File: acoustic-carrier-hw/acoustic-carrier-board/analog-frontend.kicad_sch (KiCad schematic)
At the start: 101 parts, among them J1001 BWU.FL-IPEX1, J1002 BWU.FL-IPEX1, J1003 BWU.FL-IPEX1, J1004 BWU.FL-IPEX1, J1005 BWU.FL-IPEX1, J1006 BWU.FL-IPEX1, J1007 8P8C_Shielded, J1008 BWU.FL-IPEX1, J1009 BWU.FL-IPEX1, J1010 BWU.FL-IPEX1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

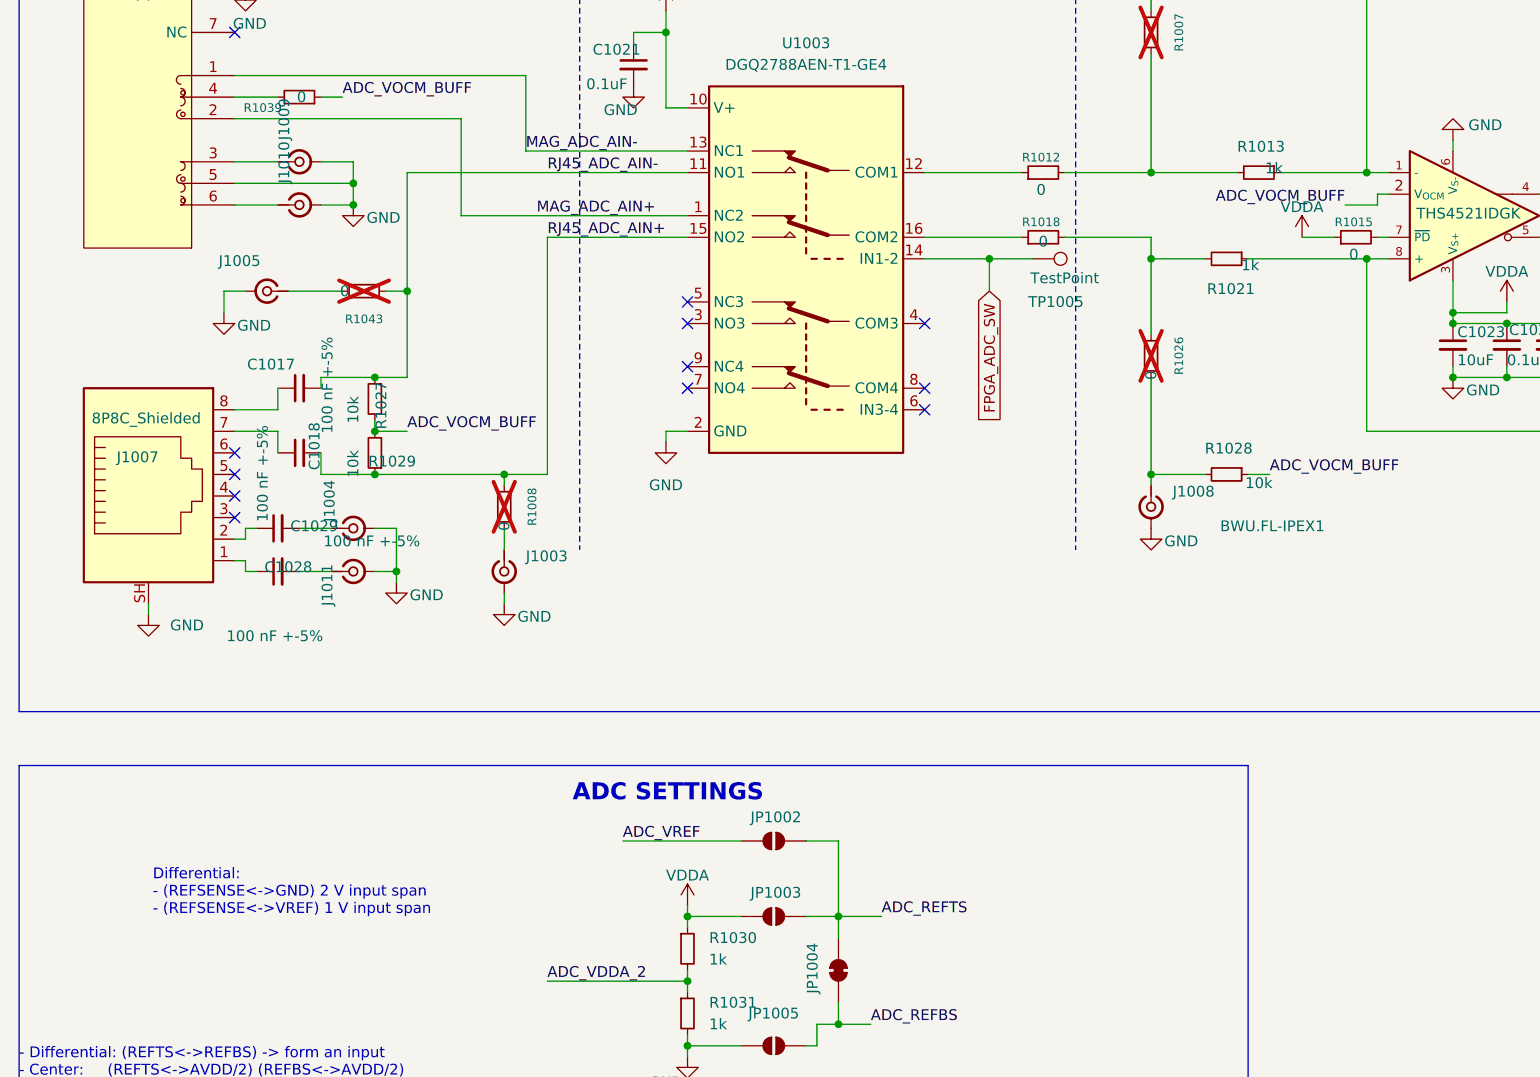
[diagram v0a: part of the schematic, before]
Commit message: [carrier] finished final review, (next) posting to linkedin, start working on analog front-end board
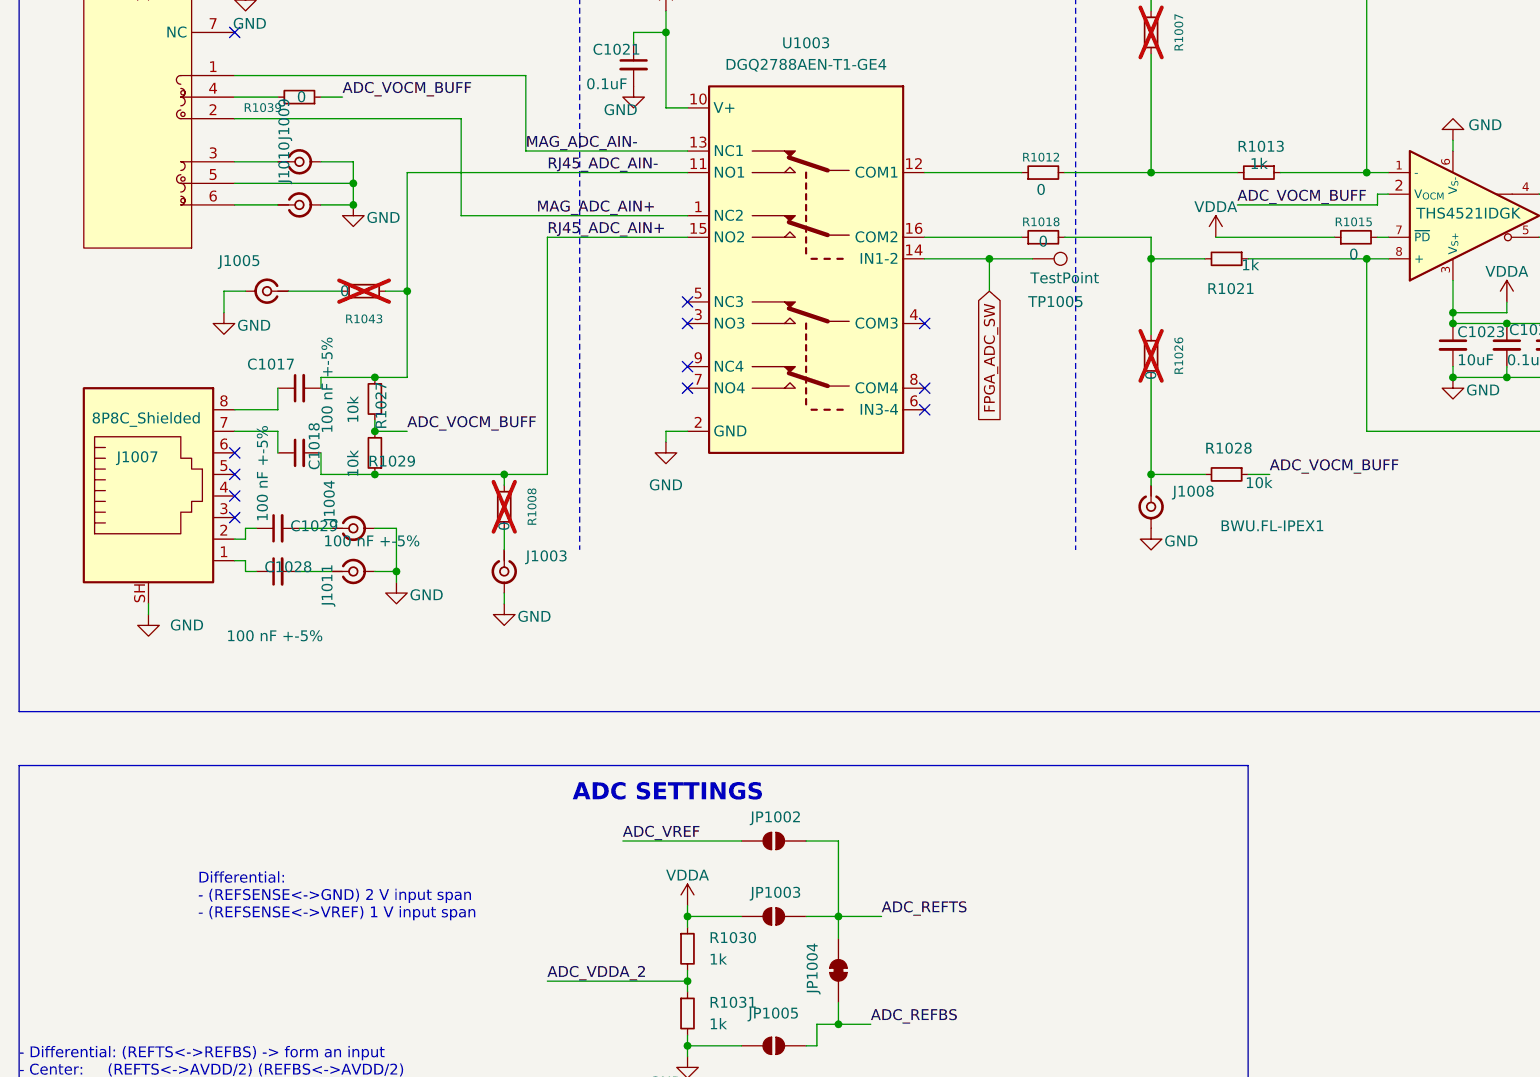
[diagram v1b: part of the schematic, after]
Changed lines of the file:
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@@
 	(text "Differential: \n- (REFSENSE<->GND) 2 V input span\n- (REFSENSE<->VREF) 1 V input span"
 		(exclude_from_sim no)
-		(at 29.718 168.656 0)
+		(at 35.052 169.164 0)
 		(effects
 			(font
@@
 	(wire
 		(pts
-			(xy 165.1 91.44) (xy 168.91 91.44)
+			(xy 154.94 91.44) (xy 168.91 91.44)
 		)
 		(stroke
@@
 	(wire
 		(pts
-			(xy 170.18 87.63) (xy 173.99 87.63)
+			(xy 157.48 87.63) (xy 173.99 87.63)
 		)
 		(stroke
@@
 	)
 	(label "ADC_VOCM_BUFF"
-		(at 170.18 87.63 180)
+		(at 157.48 87.63 0)
 		(effects
 			(font
 				(size 1.27 1.27)
 			)
-			(justify right bottom)
+			(justify left bottom)
 		)
 	)
@@
 		)
 		(property "Value" "1k"
-			(at 161.798 83.312 90)
+			(at 160.02 82.804 90)
 			(effects
 				(font
@@
 	(symbol
 		(lib_id "power:VDDA")
-		(at 165.1 91.44 0)
+		(at 154.94 91.44 0)
 		(unit 1)
 		(exclude_from_sim no)
@@
 		(dnp no)
 		(property "Reference" "#PWR01046"
-			(at 165.1 95.25 0)
+			(at 154.94 95.25 0)
 			(effects
 				(font
@@
 		)
 		(property "Value" "VDDA"
-			(at 165.1 87.884 0)
+			(at 154.94 87.884 0)
 			(effects
 				(font
@@
 		)
 		(property "Footprint" ""
-			(at 165.1 91.44 0)
+			(at 154.94 91.44 0)
 			(effects
 				(font
@@
 		)
 		(property "Datasheet" ""
-			(at 165.1 91.44 0)
+			(at 154.94 91.44 0)
 			(effects
 				(font
@@
 		)
 		(property "Description" "Power symbol creates a global label with name \"VDDA\""
-			(at 165.1 91.44 0)
+			(at 154.94 91.44 0)
 			(effects
 				(font

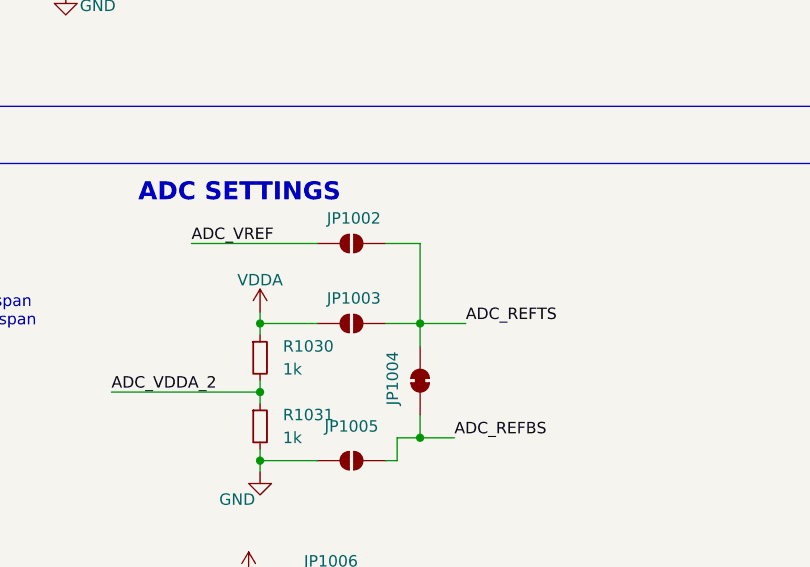
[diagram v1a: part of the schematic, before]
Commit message: [carrier] finished for production (next) reroute the LPDDR3, with appropriate CMD-CTRL bus delays, and change banks for command-control
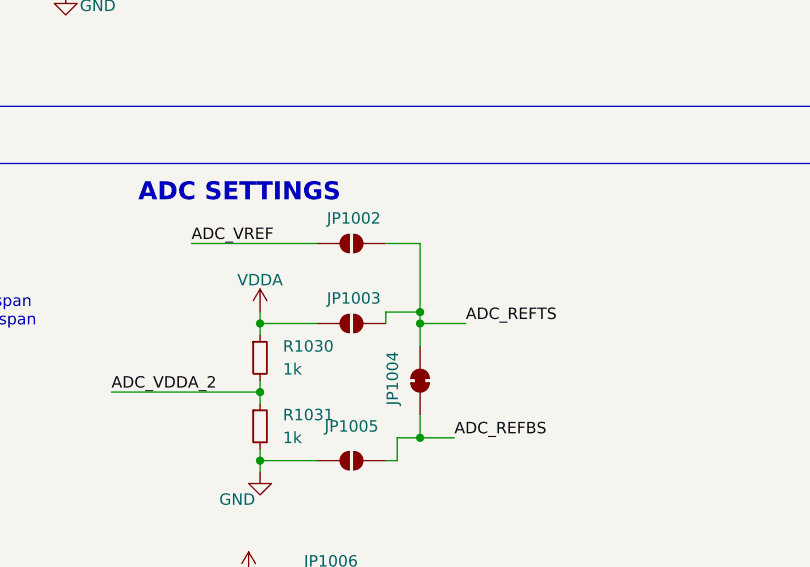
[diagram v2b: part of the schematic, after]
